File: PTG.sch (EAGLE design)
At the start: 95 parts, among them IC1 TPS62120, IC2 PIC32MK1024MCF064-I_PT, IC3 LT1762EMS8-5PBF, IC4 TPS561208DDCR, IC5 LT1762EMS8-5PBF, J1 STX-3100-5N, J2 RCJ-01X_PHONO_SINGLE, U4 PCM1748E/2K, X1 22-23-2041, Y1 EXTERNALCRYSTAL

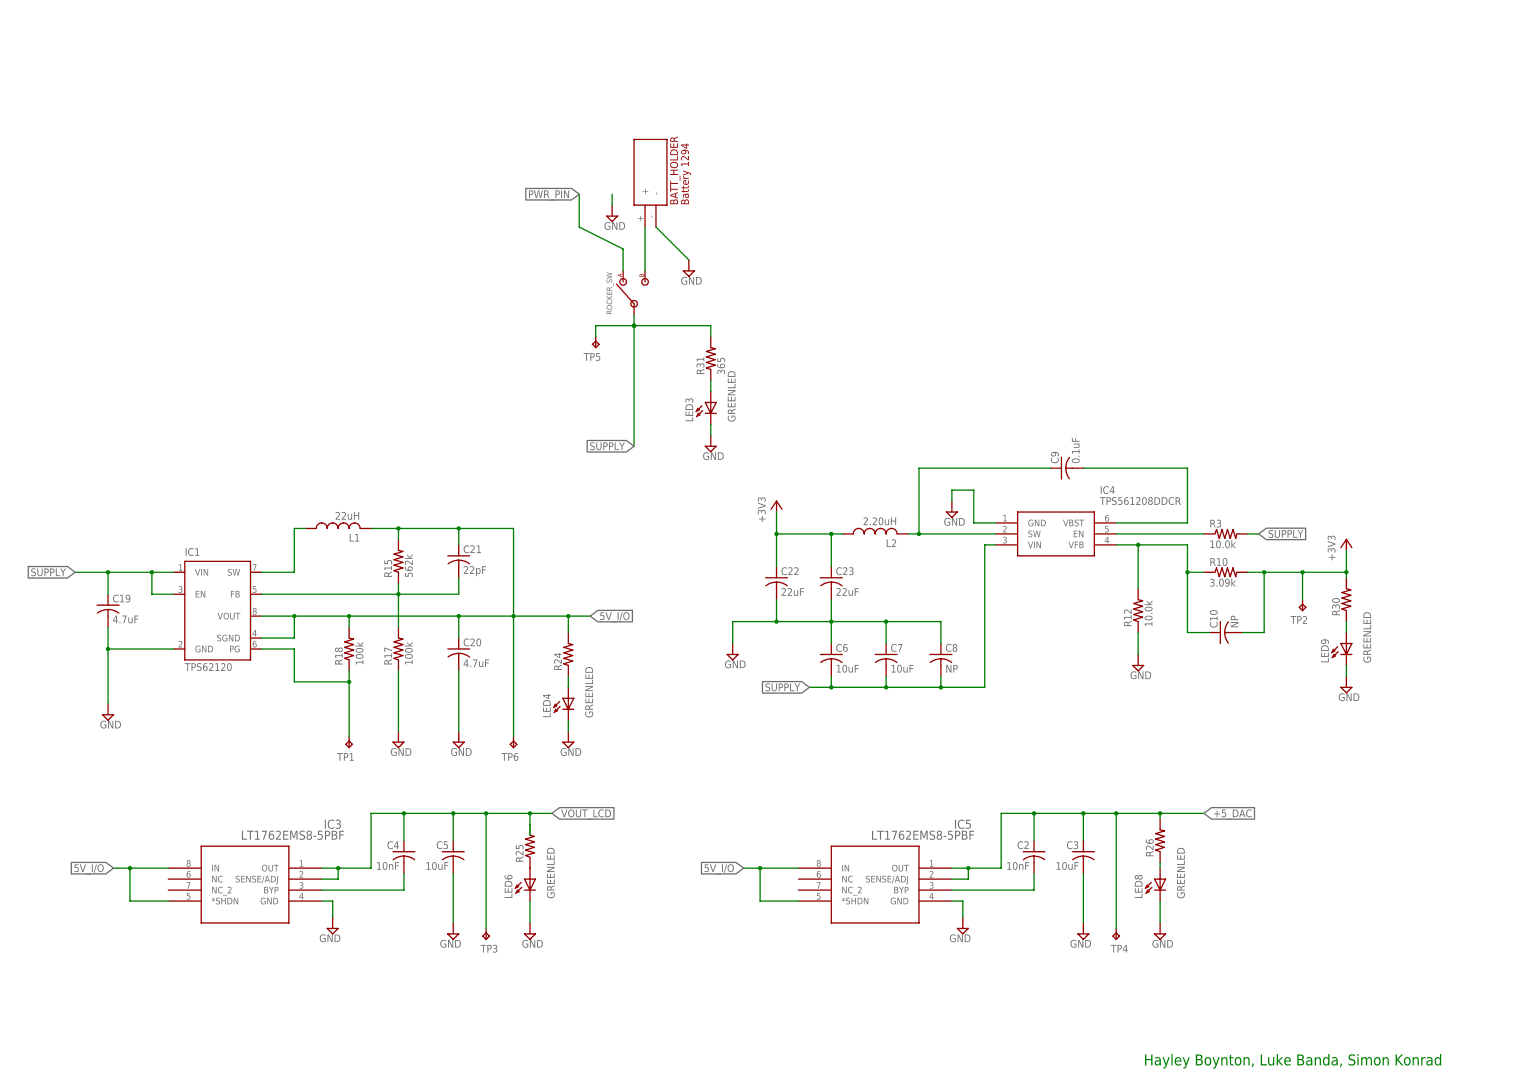
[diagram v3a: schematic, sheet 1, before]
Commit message: changes from meeting, added logos, changed test points, changed ground plane
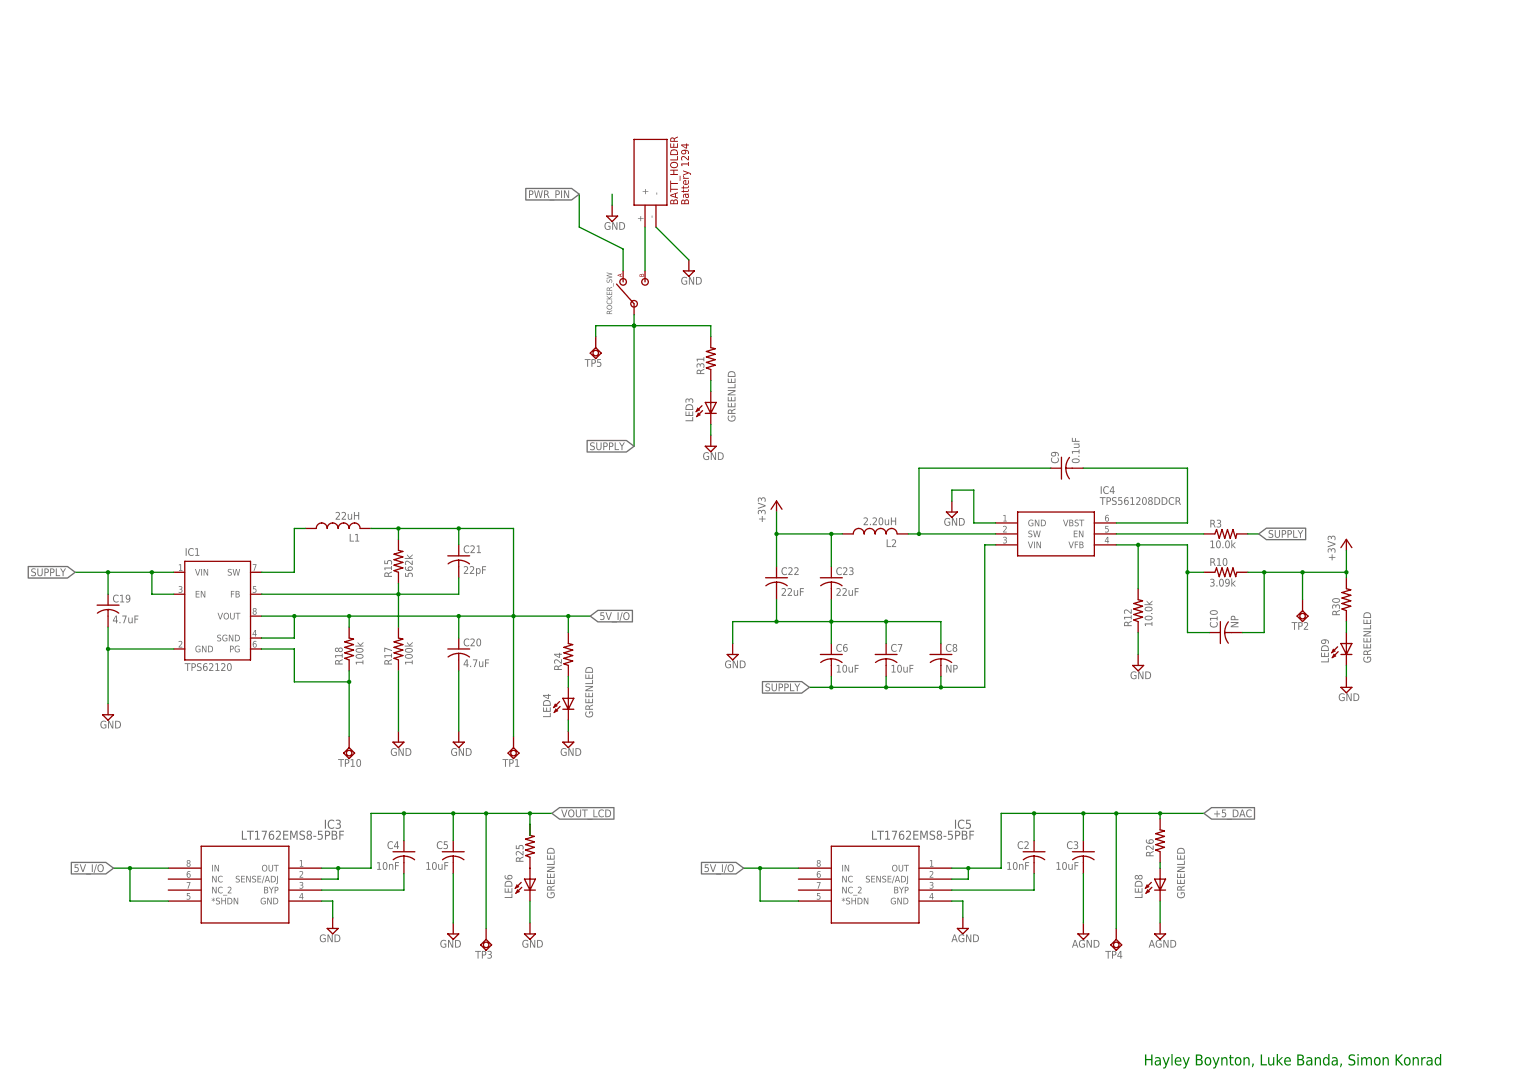
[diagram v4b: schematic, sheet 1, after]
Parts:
- removed TP11: TPTP20SQ, testpad:TPTP20SQ
- added TP8: TPSQTP20SQD, testpad:TPSQTP20SQD
- R31: value 365 -> (none)
- TP1, TP10, TP2, TP3, TP4, TP5, TP6, TP7, TP9: value TPTP20SQ -> TPSQTP20SQD; device testpad:TPTP20SQ -> testpad:TPSQTP20SQD
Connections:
- net 5V_I/O: now also TP1.TP; no longer TP6.TP
- net AGND: now also C17.2, C3.2, IC5.GND, LED8.-, U4.DGND
- net DAC_BCK: now also TP8.TP; no longer TP10.TP
- net DAC_LRCK: now also TP6.TP; no longer TP9.TP
- net GND: no longer C17.2, C3.2, IC5.GND, LED8.-, U4.DGND
- net PWRGOOD: now also TP10.TP; no longer TP1.TP
- net SYS_CLK: now also TP9.TP; no longer TP11.TP

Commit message: minor changes, added power inductor, but bad library
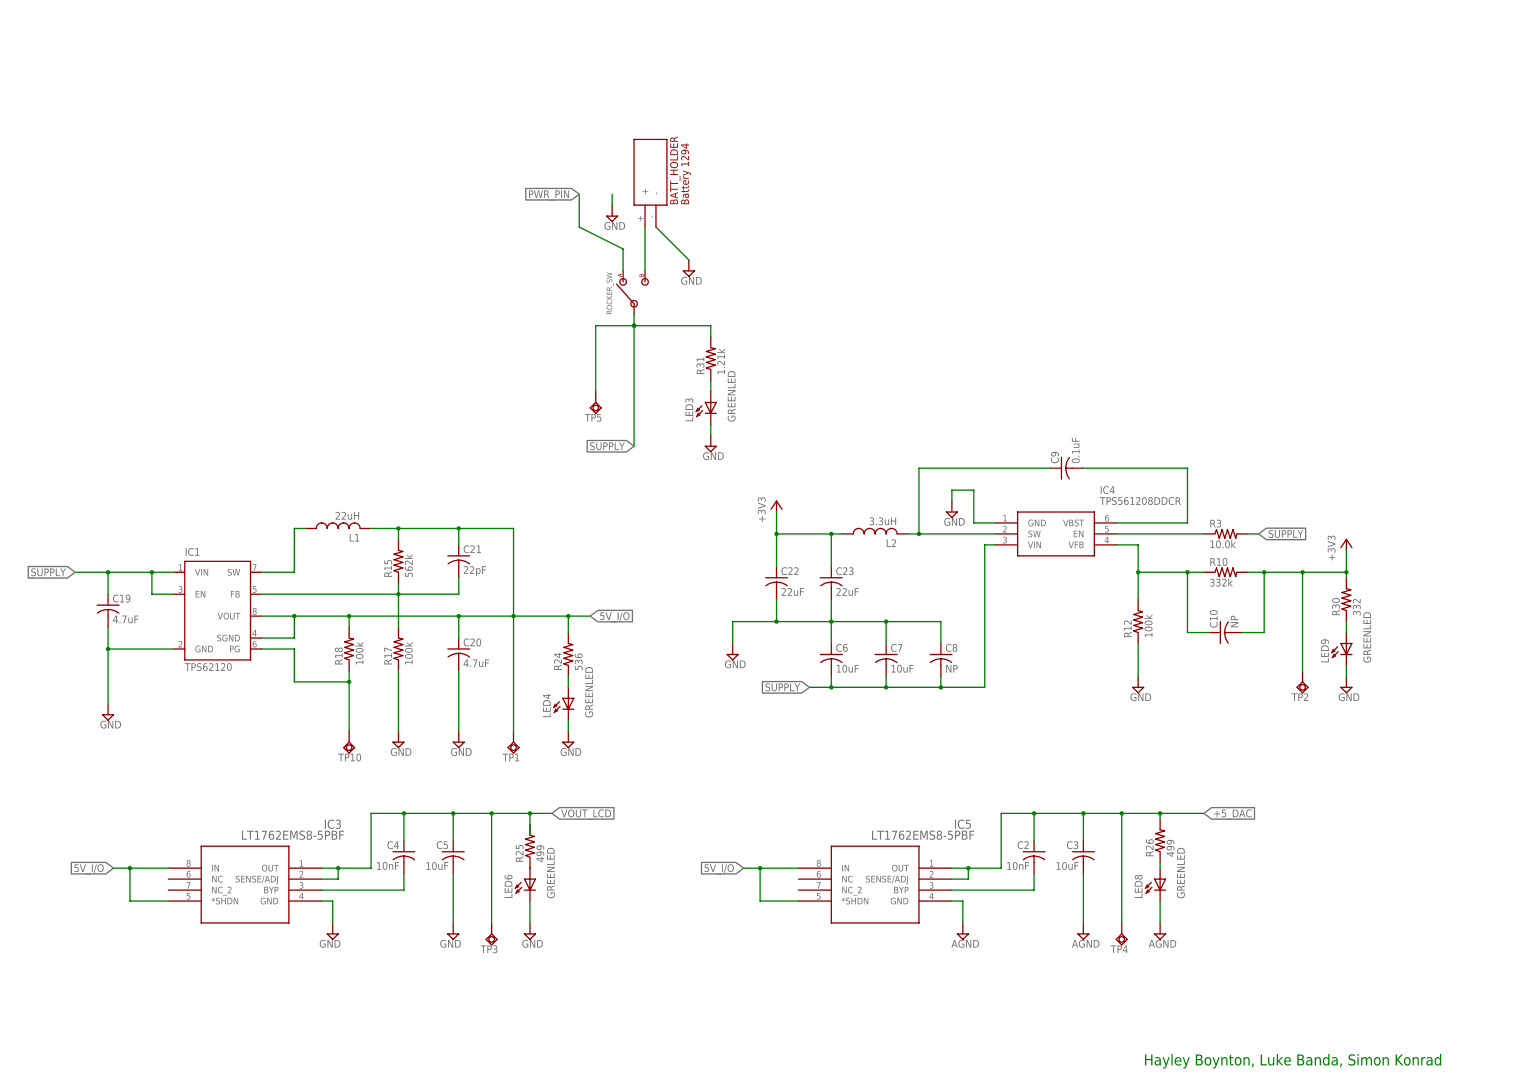
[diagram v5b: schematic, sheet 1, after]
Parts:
- L2: value 2.20uH -> 3.3uH; device NewSDR:L-US0603 -> PowerInductor:PWR_L
- R10: value 3.09k -> 332k
- R12: value 10.0k -> 100k
- R24: value (none) -> 536
- R25, R26: value (none) -> 499
- R30: value (none) -> 332
- R31: value (none) -> 1.21k
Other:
- moved on the sheet: C1, R12, TP1, TP10, TP2, TP3, TP4, TP5

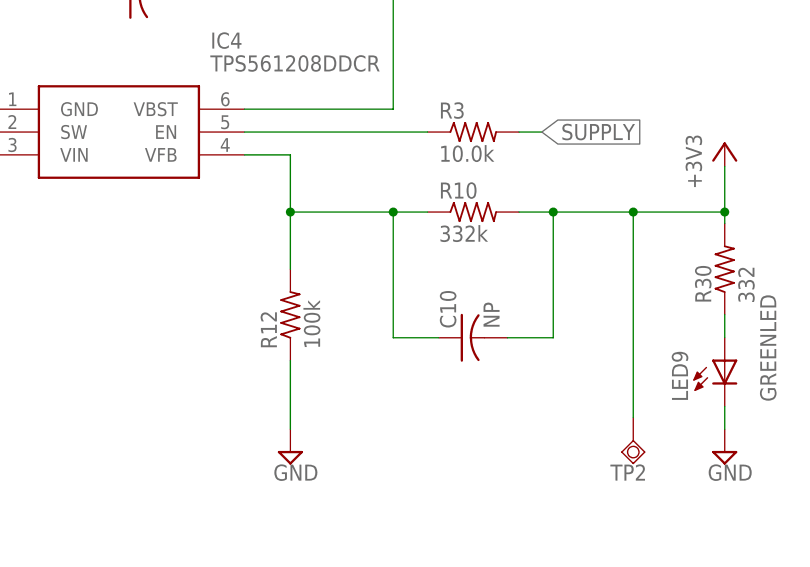
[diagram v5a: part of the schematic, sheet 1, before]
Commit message: Fixed library symbols for chassis grounds, renamed voltage nodes, switched pins on molex power conn, updated power inductors, updated through hole RCA port
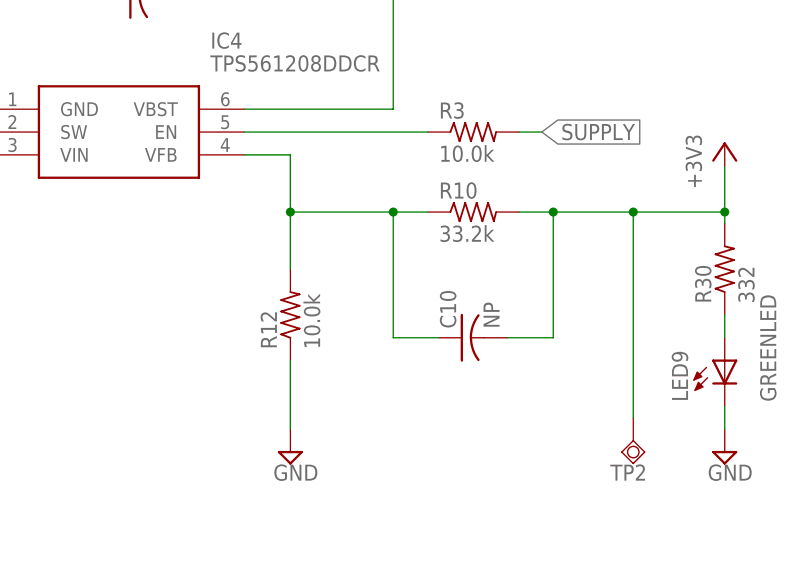
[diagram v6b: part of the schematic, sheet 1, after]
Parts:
- L2: device PowerInductor:PWR_L -> NewSDR:L-US0603
- R10: value 332k -> 33.2k
- R12: value 100k -> 10.0k
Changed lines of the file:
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@@
 <part name="R3" library="resistor" deviceset="R-US_" device="R0603" value="10.0k"/>
 <part name="SUPPLY4" library="supply2" deviceset="GND" device=""/>
-<part name="R10" library="resistor" deviceset="R-US_" device="R0603" value="332k"/>
-<part name="R12" library="resistor" deviceset="R-US_" device="R0603" value="100k"/>
+<part name="R10" library="resistor" deviceset="R-US_" device="R0603" value="33.2k"/>
+<part name="R12" library="resistor" deviceset="R-US_" device="R0603" value="10.0k"/>
 <part name="SUPPLY5" library="supply2" deviceset="GND" device=""/>
 <part name="SUPPLY6" library="supply2" deviceset="GND" device=""/>
@@
 <part name="SUPPLY11" library="supply2" deviceset="AGND" device=""/>
 <part name="SUPPLY15" library="supply2" deviceset="AGND" device=""/>
-<part name="L2" library="PowerInductor" deviceset="PWR_L" device="" value="3.3uH"/>
+<part name="L2" library="NewSDR" deviceset="L-US" device="0603" value="3.3uH"/>
 </parts>
 <sheets>

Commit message: correct file upload
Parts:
- removed BATT_HOLDER: BATTERY_HOLDER, BattHolder:BATTERY_HOLDER
- removed BUTTON1, BUTTON2, BUTTON3, BUTTON4: BUTTON-DPDT-7MM, button-dpdt-7mm:BUTTON-DPDT-7MM
- removed DIS1: NHD-0216K3Z-FL-GBW-V3, realdisplay:NHD-0216K3Z-FL-GBW-V3
- removed ENC1: ENCODERENCODER, ENCODER_PTG:ENCODERENCODER
- removed IC5: LT1762EMS8-5PBF, LDO:LT1762EMS8-5PBF
- removed ROCKER_SW: POWERSWITCH, RockerSwitch:POWERSWITCH
- removed U4: PCM1748E/2K, PCM1748:PCM1748E/2K
- added BH1: BATTERY_HOLDER, Batt_Holder:BATTERY_HOLDER
- added D1: NHD-0216K3Z-GBW-V3, NHD-0216K3Z-FL-GBW-V3:NHD-0216K3Z-GBW-V3
- added IC6, IC7: LT1762, LT1762:LT1762
- added J3: 22-27-2021-02, con-molex:22-27-2021-02
- added SW1: ROCKER_SWITCH, Rocker_Sw:ROCKER_SWITCH
- added SW2: ENCODER, Encoder:ENCODER
- added SW3, SW4, SW5, SW6: MHPS2273N, Button:MHPS2273N
- C1, C10, C11, C12, C13, C16, C17, C24, C25, C26, C9: device rcl:C-USC0805 -> rcl:C-USC0603K
- C14, C15, C2, C21, C4: device rcl:C-USC0603 -> rcl:C-USC0603K
- C18, C5, C6, C7, C8: device rcl:C-USC0805 -> rcl:C-USC0805K
- C19, C20, C22, C23: device rcl:C-USC0603 -> rcl:C-USC0805K
- C3: value 10uF -> 10nF; device rcl:C-USC0805 -> rcl:C-USC0603K
- IC1: device texas:TPS62120 -> TPS62120:TPS62120
- IC3: value LT1762EMS8-5PBF -> PCM1748; device LDO:LT1762EMS8-5PBF -> PCM1748:PCM1748
- IC4: value TPS561208DDCR -> TPS561208; device TPS561208DDCR:TPS561208DDCR -> TPS561208:TPS561208
- J1: value STX-3100-5N -> STX31005NB; device NewSDR:STX-3100-5N -> STX31005NB:STX31005NB
- J2: value RCJ-01X_PHONO_SINGLE -> RCJ-01X; device RCA:RCJ-01X_PHONO_SINGLE -> RCJ-01X:RCJ-01X
- L1, L2: device NewSDR:L-US0603 -> VLCF4020Inductor:VLCF4020_INDUCTOR
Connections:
- removed net +5_DAC: C17.1, C2.1, C3.1, IC5.OUT, IC5.SENSE/ADJ, R26.2, TP4.TP, U4.VCC
- removed net 5V_I/O: C20.1, C21.1, IC1.SGND, IC1.VOUT, IC3.*SHDN, IC3.IN, IC5.*SHDN, IC5.IN, L1.2, R15.2, R18.2, R24.2, TP1.TP
- removed net PWR_PIN: ROCKER_SW.1
- removed net SW-B: BATT_HOLDER.+, ROCKER_SW.3
- removed net VOUT_LCD: C4.1, C5.1, DIS1.VDD, IC3.OUT, IC3.SENSE/ADJ, R25.2, TP3.TP
- new net +5V5: C20.1, C21.1, IC1.SGND, IC1.VOUT, IC6.!SHDN, IC6.IN, IC7.!SHDN, IC7.IN, L1.2, R15.2, R18.2, R24.2, TP1.TP
- new net +5V_DAC: C17.1, C2.1, C3.1, IC3.VCC, IC6.OUT, IC6.SENSE/ADJ, R26.2, TP4.TP
- new net +5V_LCD: C4.1, C5.1, D1.VDD, IC7.OUT, IC7.SENSE/ADJ, R25.2, TP3.TP
- new net N$29: BH1.POS, SW1.1
- new net N$30: J3-2.S, SW1.3
- net !DAC_CS: now also IC3.ML; no longer U4.ML
- net +3V3: now also IC3.VDD, SW3.2, SW3.5, SW4.2, SW4.5, SW5.2, SW5.5, SW6.2, SW6.5; no longer BUTTON1.2, BUTTON1.5, BUTTON2.2, BUTTON2.5, BUTTON3.2, BUTTON3.5, BUTTON4.2, BUTTON4.5, U4.VDD
- net AGND: now also IC3.AGND, IC3.DGND, IC6.GND; no longer IC5.GND, U4.AGND, U4.DGND
- net BUTTON1: now also SW3.3, SW3.4; no longer BUTTON1.3, BUTTON1.4
- net BUTTON2: now also SW4.3, SW4.4; no longer BUTTON2.3, BUTTON2.4
- net BUTTON3: now also SW5.3, SW5.4; no longer BUTTON3.3, BUTTON3.4
- net BUTTON4: now also SW6.3, SW6.4; no longer BUTTON4.3, BUTTON4.4
- net DAC_BCK: now also IC3.BCK; no longer U4.BCK
- net DAC_DATA: now also IC3.DATA; no longer U4.DATA
- net DAC_LRCK: now also IC3.LRCLK; no longer U4.LRCK
- net DAC_SPI_CLK: now also IC3.MC; no longer U4.MC
- net DAC_SPI_DATA: now also IC3.MD; no longer U4.MD
- net DAC_ZEROH: now also IC3.ZERO_R/ZEROA; no longer U4.ZEROR/ZEROA
- net DAC_ZEROL: now also IC3.ZERO_L/NA; no longer U4.ZEROL/NA
- net DIS_!CS: now also D1.SPISS; no longer DIS1.SPISS
- net DIS_SCK: now also D1.SCK/SCL; no longer DIS1.SCK/SCL
- net DIS_SDI: now also D1.SDI/SDA; no longer DIS1.SDI/SDA
- net ENC_A: now also SW2.A; no longer ENC1.P_A
- net ENC_B: now also SW2.B; no longer ENC1.P_B
- net GND: now also BH1.NEG, D1.VSS, IC7.GND, J2.1, J3-1.S, SW1.G, SW2.C, SW2.G; no longer BATT_HOLDER.-, DIS1.VSS, ENC1.P_C, IC3.GND, J2G$1.SH
- net N$19: now also IC3.VCOM; no longer U4.VCOM
- net N$23: now also IC7.BYP; no longer IC3.BYP
- net N$9: now also IC6.BYP; no longer IC5.BYP
- net SIGNAL_L: now also IC3.VOUT_L; no longer U4.VOUTL
- net SIGNAL_R: now also IC3.VOUT_R; no longer U4.VOUTR
- net SUPPLY: now also SW1.2; no longer ROCKER_SW.2
- net SYS_CLK: now also IC3.SCK; no longer U4.SCK
- net TRIGGER: now also J2.2; no longer J2G$1.PIN
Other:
- moved on the sheet: C1, C10, C11, C14, C15, C16, C17, C18, C19, C2, C20, C21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
